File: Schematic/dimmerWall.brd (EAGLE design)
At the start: 60 x 60 mm, 22 parts, among them Q1 IRF840, T1 BC547

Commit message: Use better schematic
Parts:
- added PROG: (no value), con-lstb:MA03-1
- C1, C2: device rcl:E2,5-6 -> rcl:TT2D4L
- moved C2 10.2 mm to (3.81, 17.8), flipped to the bottom, turned to 180 degrees
- moved C1 3.59 mm to (8.89, 17.8), flipped to the bottom
- moved T1 2.54 mm to (5.08, 30.5)
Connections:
- new net N$11: PROG.1, U$1.UTXD
- new net N$12: PROG.2, U$1.URXD
- net GND: now also PROG.3
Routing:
- net +5V: track 12.7 -> 5.08 mm
- net GND: track 97.8 -> 92.7 mm
- net +3V3: track 38.6 -> 36.1 mm
- net N$5: track 0.69 -> 3.23 mm
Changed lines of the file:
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@@
 <element name="R6" library="rcl" package="0207/12" value="51k" x="16.002" y="27.94" rot="R337"/>
 <element name="B2" library="rectifier" package="2KBP" value="" x="43.18" y="27.94" rot="R270"/>
-<element name="C1" library="rcl" package="E2,5-6" value="10u/16" x="6.35" y="15.24" rot="R180"/>
-<element name="C2" library="rcl" package="E2,5-6" value="10u/16" x="3.81" y="27.94"/>
+<element name="C1" library="rcl" package="TT2D4L" value="10u/16" x="8.89" y="17.78" rot="MR180"/>
+<element name="C2" library="rcl" package="TT2D4L" value="10u/16" x="3.81" y="17.78" rot="MR180"/>
 <element name="L1" library="rcl" package="0204/5" value="330n" x="6.604" y="22.86"/>
 <element name="U$1" library="esp8266modules" package="ESP-03" value="ESP8266" x="22.86" y="17.78" rot="R270"/>
-<element name="T1" library="transistor" package="TO92" value="BC547" x="7.62" y="30.48" rot="R270"/>
+<element name="T1" library="transistor" package="TO92" value="BC547" x="5.08" y="30.48" rot="R270"/>
 <element name="D1" library="diode" package="DO41-7.6" value="1N5817-B" x="6.35" y="25.4" rot="R180"/>
 <element name="D4" library="diode" package="DO41-7.6" value="1N4148" x="6.35" y="20.32"/>
@@
 </element>
 <element name="U$2" library="smps" package="SMPS" value="SMPS" x="20.32" y="20.32" rot="R180"/>
+<element name="PROG" library="con-lstb" package="MA03-1" value="" x="12.7" y="12.7" rot="R90">
+<attribute name="MPN" value="" x="12.7" y="12.7" size="1.778" layer="27" rot="R90" display="off"/>
+<attribute name="OC_FARNELL" value="unknown" x="12.7" y="12.7" size="1.778" layer="27" rot="R90" display="off"/>
+<attribute name="MF" value="" x="12.7" y="12.7" size="1.778" layer="27" rot="R90" display="off"/>
+<attribute name="OC_NEWARK" value="unknown" x="12.7" y="12.7" size="1.778" layer="27" rot="R90" display="off"/>
+</element>
 </elements>
 <signals>
@@
 <wire x1="7.62" y1="25.4" x2="10.16" y2="25.4" width="0.254" layer="16"/>
 <wire x1="10.16" y1="25.4" x2="12.7" y2="25.4" width="0.254" layer="16"/>
-<wire x1="7.62" y1="15.24" x2="7.62" y2="25.4" width="0.254" layer="16"/>
 <wire x1="12.7" y1="25.4" x2="12.7" y2="27.94" width="0.254" layer="16"/>
 <wire x1="12.7" y1="27.94" x2="27.94" y2="27.94" width="0.254" layer="16"/>
@@
 <via x="27.94" y="22.86" extent="1-16" drill="0.6" diameter="0.254" shape="square"/>
 <wire x1="27.94" y1="22.86" x2="27.94" y2="27.94" width="0.254" layer="16"/>
+<wire x1="7.62" y1="17.78" x2="7.62" y2="25.4" width="0.4064" layer="16"/>
 </signal>
 <signal name="GND">
@@
 <wire x1="38.1" y1="40.64" x2="38.1" y2="35.56" width="0.254" layer="16"/>
 <wire x1="38.1" y1="35.56" x2="43.18" y2="35.56" width="0.254" layer="16"/>
-<wire x1="7.62" y1="29.21" x2="7.62" y2="27.94" width="0.254" layer="16"/>
-<wire x1="5.08" y1="27.94" x2="7.62" y2="27.94" width="0.254" layer="16"/>
-<wire x1="5.08" y1="15.24" x2="5.08" y2="27.94" width="0.254" layer="16"/>
-<wire x1="12.7" y1="17.78" x2="12.7" y2="15.24" width="0.254" layer="16"/>
-<wire x1="12.7" y1="15.24" x2="12.7" y2="12.7" width="0.254" layer="16"/>
-<wire x1="12.7" y1="12.7" x2="5.08" y2="12.7" width="0.254" layer="16"/>
-<wire x1="5.08" y1="12.7" x2="5.08" y2="15.24" width="0.254" layer="16"/>
-<wire x1="33.02" y1="15.24" x2="12.7" y2="15.24" width="0.254" layer="16"/>
-<wire x1="12.7" y1="12.7" x2="12.7" y2="10.16" width="0.254" layer="16"/>
+<wire x1="12.7" y1="17.78" x2="12.7" y2="15.494" width="0.254" layer="16"/>
+<wire x1="33.02" y1="15.24" x2="15.24" y2="15.24" width="0.254" layer="16"/>
+<wire x1="12.7" y1="15.24" x2="15.24" y2="15.24" width="0.254" layer="16"/>
 <wire x1="43.18" y1="33.655" x2="43.18" y2="35.56" width="0.254" layer="16"/>
 <wire x1="38.1" y1="35.56" x2="35.56" y2="35.56" width="0.254" layer="16"/>
 <wire x1="35.56" y1="35.56" x2="35.56" y2="15.24" width="0.254" layer="16"/>
 <wire x1="35.56" y1="15.24" x2="33.02" y2="15.24" width="0.254" layer="16"/>
+<wire x1="15.66" y1="10.38" x2="15.24" y2="10.38" width="0.254" layer="1"/>
+<wire x1="15.24" y1="10.38" x2="15.24" y2="10.16" width="0.254" layer="1"/>
+<via x="15.24" y="10.16" extent="1-16" drill="0.6" diameter="0.254" shape="square"/>
+<wire x1="15.24" y1="10.16" x2="15.24" y2="15.24" width="0.254" layer="16"/>
+<wire x1="5.08" y1="15.24" x2="12.7" y2="15.24" width="0.4064" layer="16"/>
+<wire x1="12.7" y1="15.24" x2="12.7" y2="15.494" width="0.4064" layer="16"/>
+<wire x1="10.16" y1="17.78" x2="12.7" y2="17.78" width="0.4064" layer="16"/>
+<wire x1="5.08" y1="17.78" x2="5.08" y2="15.24" width="0.4064" layer="16"/>
+<wire x1="5.08" y1="17.78" x2="5.08" y2="29.21" width="0.4064" layer="16"/>
+<contactref element="PROG" pad="3"/>
 <wire x1="63.2206" y1="44.2468" x2="63.2206" y2="50.7492" width="0" layer="19" extent="1-1"/>
 <wire x1="63.2206" y1="39.3192" x2="63.2206" y2="44.2468" width="0" layer="19" extent="1-1"/>
@@
 <wire x1="63.2206" y1="12.2428" x2="63.2206" y2="18.7452" width="0" layer="19" extent="1-1"/>
 <wire x1="43.18" y1="33.655" x2="63.2206" y2="32.8168" width="0" layer="19" extent="1-1"/>
-<wire x1="15.66" y1="10.38" x2="15.24" y2="10.38" width="0.254" layer="1"/>
-<wire x1="15.24" y1="10.38" x2="15.24" y2="10.16" width="0.254" layer="1"/>
-<via x="15.24" y="10.16" extent="1-16" drill="0.6" diameter="0.254" shape="square"/>
-<wire x1="15.24" y1="10.16" x2="12.7" y2="10.16" width="0.254" layer="16"/>
+<wire x1="12.7" y1="15.24" x2="15.24" y2="15.24" width="0" layer="19" extent="16-16"/>
 </signal>
 <signal name="N$17">
@@
 <contactref element="R4" pad="2"/>
 <contactref element="T1" pad="3"/>
-<wire x1="0" y1="33.02" x2="7.62" y2="33.02" width="0.254" layer="16"/>
-<wire x1="7.62" y1="33.02" x2="20.32" y2="33.02" width="0.254" layer="16"/>
+<wire x1="0" y1="33.02" x2="5.08" y2="33.02" width="0.254" layer="16"/>
+<wire x1="5.08" y1="33.02" x2="20.32" y2="33.02" width="0.254" layer="16"/>
 <wire x1="20.32" y1="33.02" x2="20.32" y2="30.48" width="0.254" layer="16"/>
-<wire x1="7.62" y1="31.75" x2="7.62" y2="33.02" width="0.254" layer="16"/>
+<wire x1="5.08" y1="31.75" x2="5.08" y2="33.02" width="0.254" layer="16"/>
 </signal>
 <signal name="N$1">
@@
 <contactref element="D4" pad="C"/>
 <wire x1="2.54" y1="20.32" x2="0" y2="20.32" width="0.4064" layer="16"/>
-<wire x1="0" y1="20.32" x2="0" y2="27.94" width="0.254" layer="16"/>
-<wire x1="0" y1="27.94" x2="2.54" y2="27.94" width="0.254" layer="16"/>
+<wire x1="2.54" y1="17.78" x2="2.54" y2="20.32" width="0.4064" layer="16"/>
 </signal>
 <signal name="N$4">
@@
 <contactref element="T1" pad="2"/>
 <contactref element="R6" pad="1"/>
-<wire x1="9.525" y1="30.48" x2="10.15679375" y2="30.48" width="0.254" layer="16"/>
+<wire x1="6.985" y1="30.48" x2="10.15679375" y2="30.48" width="0.254" layer="16"/>
 <wire x1="10.15679375" y1="30.48" x2="10.15679375" y2="30.421140625" width="0.254" layer="16"/>
 </signal>
@@
 <wire x1="21.847203125" y1="25.4" x2="21.847203125" y2="25.45885625" width="0.254" layer="16"/>
 </signal>
+<signal name="N$11">
+<contactref element="U$1" pad="UTXD"/>
+<contactref element="PROG" pad="1"/>
+<wire x1="12.7" y1="10.16" x2="19.66" y2="10.38" width="0" layer="19" extent="1-1"/>
+</signal>
+<signal name="N$12">
+<contactref element="PROG" pad="2"/>
+<contactref element="U$1" pad="URXD"/>
+<wire x1="12.7" y1="12.7" x2="21.66" y2="10.38" width="0" layer="19" extent="1-1"/>
+</signal>
 </signals>

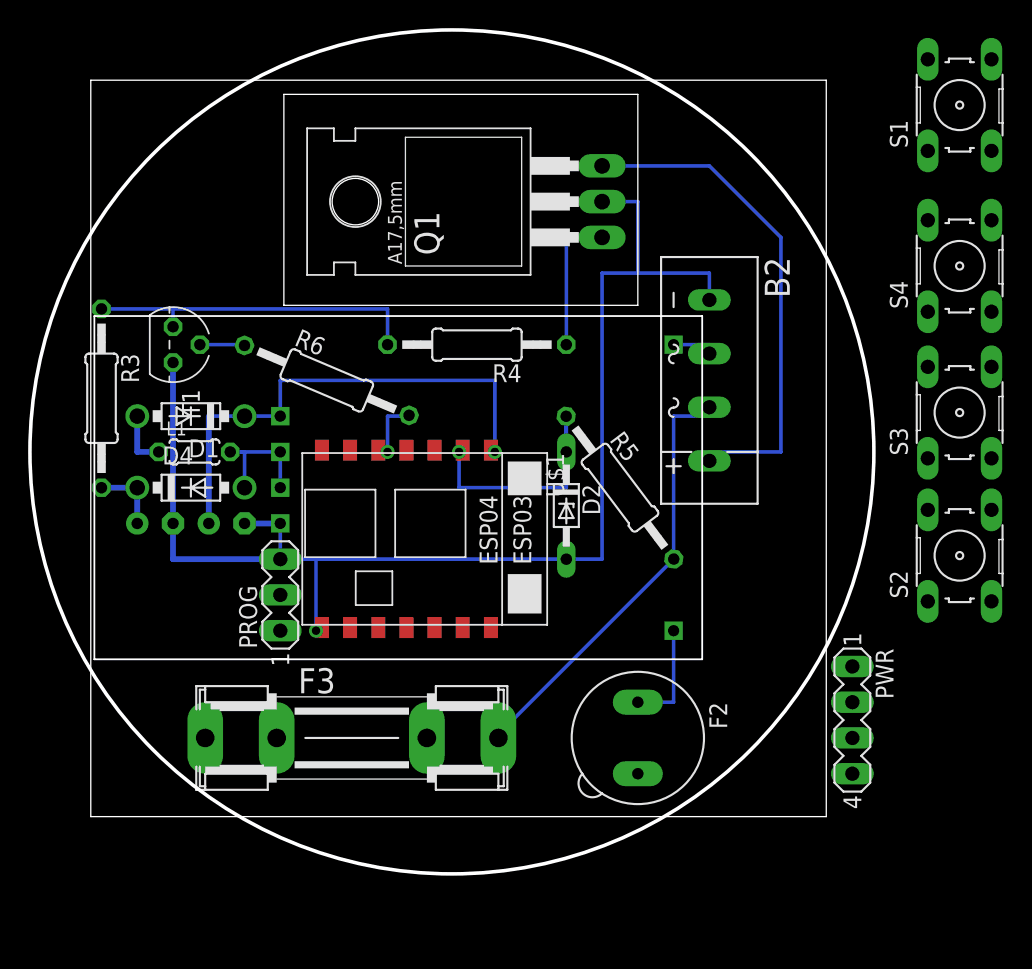
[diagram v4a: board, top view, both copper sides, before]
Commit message: Connect correct pins for boot mode
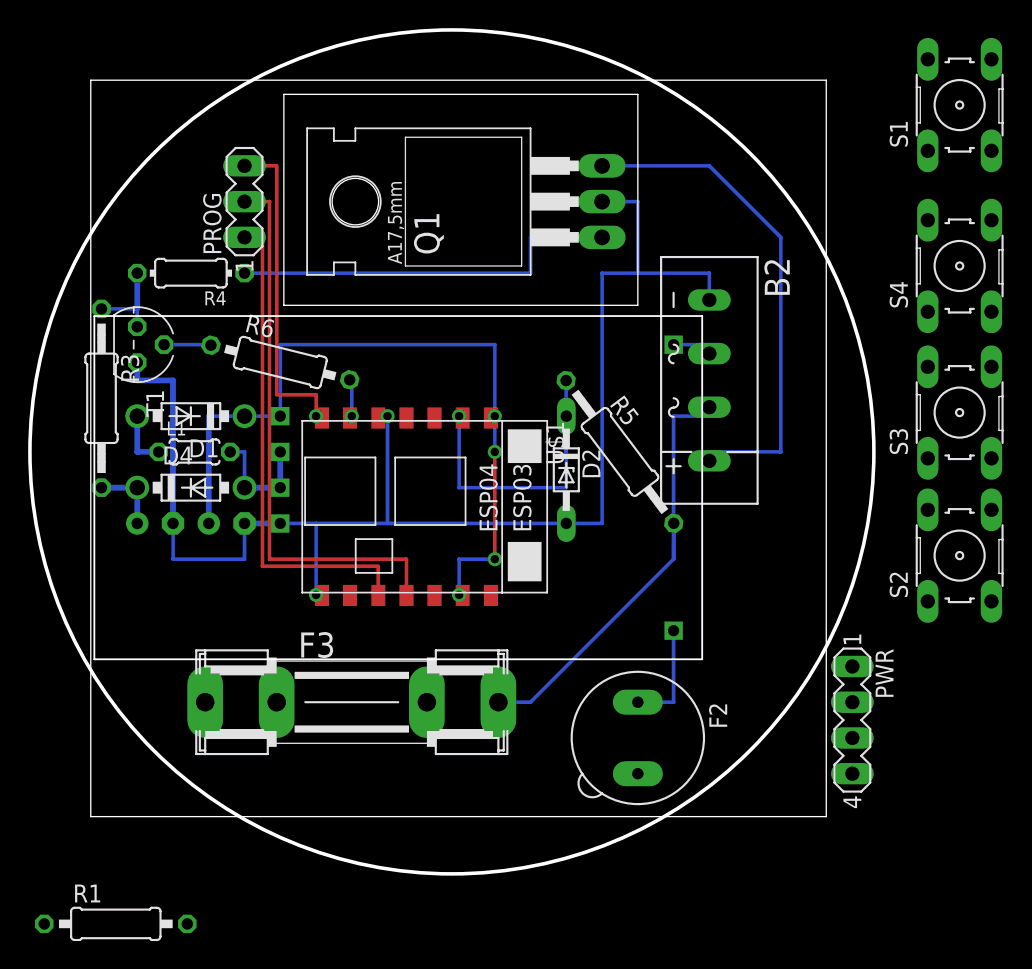
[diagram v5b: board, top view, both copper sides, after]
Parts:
- added R1: 470, rcl:0207/10
- R4: device rcl:0207/12 -> rcl:0204/7
- R6: device rcl:0207/12 -> rcl:0207/10
- moved PROG 28.1 mm to (10.2, 40.6)
- moved R4 20.9 mm to (6.35, 35.6)
- moved R6 3.54 mm to (12.7, 29.2), turned to 346 degrees
- moved F3 2.54 mm to (17.8, 5.08)
- moved T1 2.54 mm to (2.54, 30.5)
- moved D2 2.54 mm to (33.0, 21.6)
- moved R5 2.54 mm to (36.8, 22.9)
- moved U$1 2.29 mm to (22.9, 20.1)
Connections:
- new net N$18: R1.2, S1.3, S1.4, S2.3, S2.4, S3.3, S3.4, S4.3, S4.4
- net +3V3: now also U$1.CH_PD
- net GND: now also R1.1, U$1.GPIO15; no longer PROG.3, S1.3, S1.4, S2.3, S2.4, S3.3, S3.4, S4.3, S4.4
- net N$10: now also U$1.GPIO2; no longer U$1.GPIO15
- net N$13: now also PROG.3
- net N$14: now also U$1.GPIO13; no longer U$1.GPIO2
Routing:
- net N$12: track 0.00 -> 39.5 mm
- net N$11: track 0.00 -> 34.9 mm
- net N$13: track 0.00 -> 23.7 mm, vias 0 -> 1
- net +3V3: track 36.1 -> 53.9 mm, vias 1 -> 4
- net N$2: track 24.1 -> 6.35 mm
- net N$1: track 10.2 -> 27.9 mm
- net N$7: track 18.3 -> 25.7 mm
- net GND: track 92.7 -> 98.6 mm, vias 1 -> 2
- net N$10: track 4.97 -> 2.99 mm
- net N$6: track 9.65 -> 8.64 mm
- net N$17: track 31.6 -> 32.5 mm
